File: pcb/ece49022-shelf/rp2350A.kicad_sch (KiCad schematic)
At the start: 32 parts, among them J1 USB_B_Micro, J4 SM03B-SRSS-TB, SW1 SW_Push, SW2 SW_Push, U3 W25Q128JVS, U5 RP2350_60QFN, Y1 ABM8-272-T3

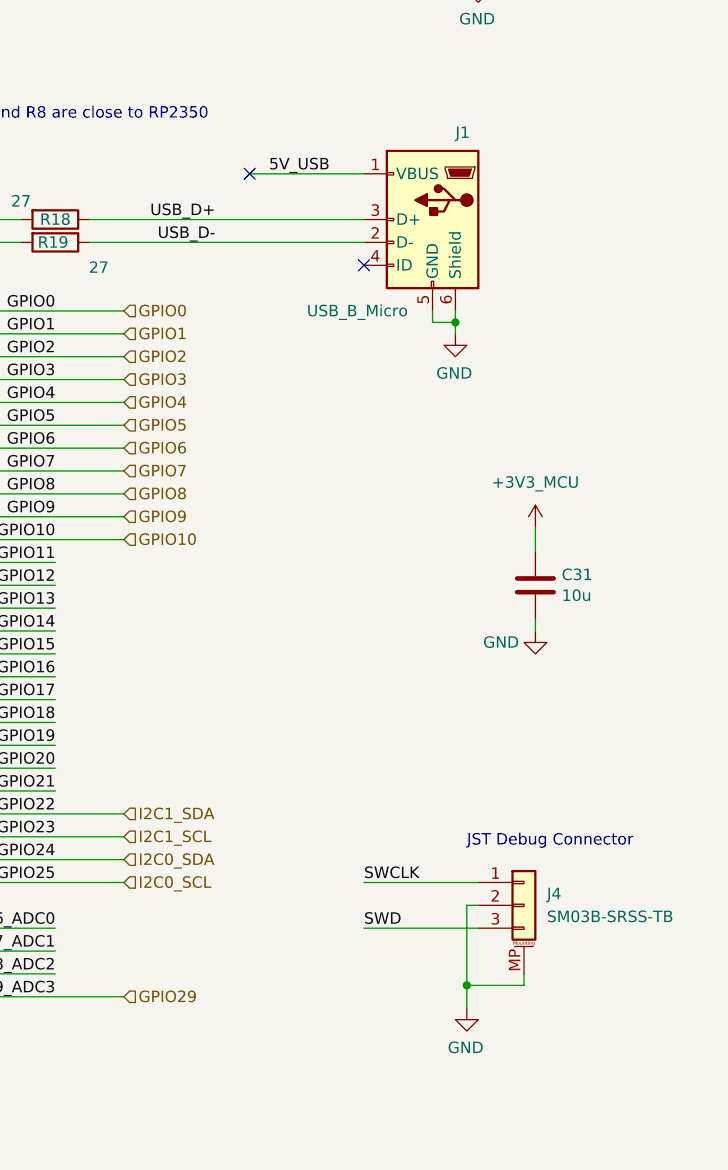
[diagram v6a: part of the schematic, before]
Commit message: new converter layout
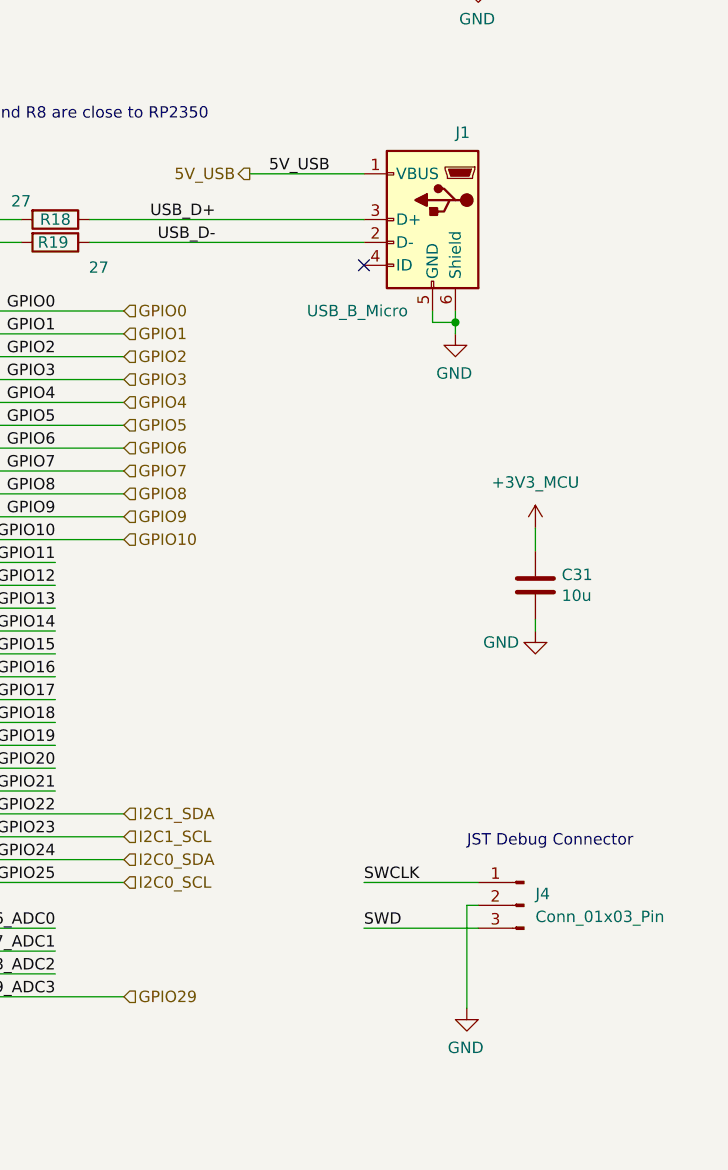
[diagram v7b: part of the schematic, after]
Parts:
- removed J4: SM03B-SRSS-TB, Connector_JST:JST_SH_SM03B-SRSS-TB_1x03-1MP_P1.00mm_Horizontal, symbol Connector_Generic_MountingPin:Conn_01x03_MountingPin
- added J4: Conn_01x03_Pin, Connector_PinHeader_2.54mm:PinHeader_1x03_P2.54mm_Vertical, symbol Connector:Conn_01x03_Pin
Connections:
- net GND: now also J4.2 (Pin_2)
- net SWCLK: now also J4.1 (Pin_1)
- net SWD: now also J4.3 (Pin_3)
- no-connect marks 2 -> 1
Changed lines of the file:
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@@
 		(color 0 0 0 0)
 	)
-	(junction
-		(at 289.56 177.8)
-		(diameter 0)
-		(color 0 0 0 0)
-	)
-	(no_connect
-		(at 265.43 87.63)
-	)
 	(no_connect
 		(at 278.13 97.79)
@@
 	(wire
 		(pts
-			(xy 289.56 177.8) (xy 289.56 180.34)
+			(xy 289.56 168.91) (xy 289.56 180.34)
 		)
 		(stroke
@@
 	(wire
 		(pts
-			(xy 289.56 168.91) (xy 289.56 177.8)
-		)
-		(stroke
-			(width 0)
-			(type default)
-		)
-	)
-	(wire
-		(pts
 			(xy 278.13 87.63) (xy 265.43 87.63)
 		)
@@
 	(wire
 		(pts
-			(xy 295.91 176.53) (xy 295.91 177.8)
-		)
-		(stroke
-			(width 0)
-			(type default)
-		)
-	)
-	(wire
-		(pts
 			(xy 233.68 52.07) (xy 245.11 52.07)
 		)
@@
 	(wire
 		(pts
-			(xy 289.56 177.8) (xy 295.91 177.8)
-		)
-		(stroke
-			(width 0)
-			(type default)
-		)
-	)
-	(wire
-		(pts
 			(xy 247.65 92.71) (xy 278.13 92.71)
 		)
@@
 		)
 	)
+	(hierarchical_label "5V_USB"
+		(shape output)
+		(at 265.43 87.63 180)
+		(effects
+			(font
+				(size 1.27 1.27)
+			)
+			(justify right)
+		)
+	)
 	(hierarchical_label "GPIO5"
 		(shape input)
@@
 	)
 	(symbol
-		(lib_id "Connector_Generic_MountingPin:Conn_01x03_MountingPin")
-		(at 295.91 168.91 0)
-		(unit 1)
-		(exclude_from_sim no)
-		(in_bom yes)
-		(on_board yes)
-		(dnp no)
-		(fields_autoplaced yes)
-		(property "Reference" "J4"
-			(at 298.45 167.64 0)
-			(effects
-				(font
-					(size 1.27 1.27)
-				)
-				(justify left)
-			)
-		)
-		(property "Value" "SM03B-SRSS-TB"
-			(at 298.45 170.18 0)
-			(effects
-				(font
-					(size 1.27 1.27)
-				)
-				(justify left)
-			)
-		)
-		(property "Footprint" "Connector_JST:JST_SH_SM03B-SRSS-TB_1x03-1MP_P1.00mm_Horizontal"
-			(at 295.91 168.91 0)
-			(effects
-				(font
-					(size 1.27 1.27)
-				)
-				(hide yes)
-			)
-		)
-		(property "Datasheet" "~"
-			(at 295.91 168.91 0)
-			(effects
-				(font
-					(size 1.27 1.27)
-				)
-				(hide yes)
-			)
-		)
-		(property "Description" ""
-			(at 295.91 168.91 0)
-			(effects
-				(font
-					(size 1.27 1.27)
-				)
-			)
-		)
-		(pin "1"
-		)
-		(pin "2"
-		)
-		(pin "3"
-		)
-		(pin "MP"
-		)
-		(instances
-			(project "ece49022-shelf"
-				(path "/cb6cb1b4-c151-4aa2-8cd7-5430288cfa02/d90a4203-0e8d-4fad-a588-f7d5681a1fb6"
-					(reference "J4")
-					(unit 1)
-				)
-			)
-		)
-	)
-	(symbol
 		(lib_name "+3V3_1")
 		(lib_id "power:+3V3")
@@
 					(unit 1)
 				)
+			)
+		)
+	)
+	(symbol
+		(lib_id "Connector:Conn_01x03_Pin")
+		(at 295.91 168.91 0)
+		(mirror y)
+		(unit 1)
+		(exclude_from_sim no)
+		(in_bom yes)
+		(on_board yes)
+		(dnp no)
+		(fields_autoplaced yes)
+		(property "Reference" "J4"
+			(at 297.18 167.6399 0)
+			(effects
+				(font
+					(size 1.27 1.27)
+				)
+				(justify right)
+			)
+		)
+		(property "Value" "Conn_01x03_Pin"
+			(at 297.18 170.1799 0)
+			(effects
+				(font
+					(size 1.27 1.27)
+				)
+				(justify right)
+			)
+		)
+		(property "Footprint" "Connector_PinHeader_2.54mm:PinHeader_1x03_P2.54mm_Vertical"
+			(at 295.91 168.91 0)
+			(effects
+				(font
+					(size 1.27 1.27)
+				)
+				(hide yes)
+			)
+		)
+		(property "Datasheet" "~"
+			(at 295.91 168.91 0)
+			(effects
+				(font
+					(size 1.27 1.27)
+				)
+				(hide yes)
+			)
+		)
+		(property "Description" "Generic connector, single row, 01x03, script generated"
+			(at 295.91 168.91 0)
+			(effects
+				(font
+					(size 1.27 1.27)
+				)
+				(hide yes)
+			)
+		)
+		(pin "1"
+		)
+		(pin "2"
+		)
+		(pin "3"
+		)
+		(instances
+			(project ""
+				(path "/cb6cb1b4-c151-4aa2-8cd7-5430288cfa02/d90a4203-0e8d-4fad-a588-f7d5681a1fb6"
+					(reference "J4")
+					(unit 1)
+				)

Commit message: stuff
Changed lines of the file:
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@@
 	(wire
 		(pts
-			(xy 228.6 143.51) (xy 243.84 143.51)
+			(xy 228.6 143.51) (xy 251.46 143.51)
 		)
 		(stroke
@@
 	(wire
 		(pts
-			(xy 228.6 151.13) (xy 243.84 151.13)
+			(xy 228.6 151.13) (xy 251.46 151.13)
 		)
 		(stroke
@@
 	(wire
 		(pts
-			(xy 228.6 148.59) (xy 243.84 148.59)
+			(xy 228.6 148.59) (xy 251.46 148.59)
 		)
 		(stroke
@@
 	(wire
 		(pts
-			(xy 228.6 156.21) (xy 243.84 156.21)
+			(xy 228.6 156.21) (xy 251.46 156.21)
 		)
 		(stroke
@@
 	(wire
 		(pts
-			(xy 228.6 146.05) (xy 243.84 146.05)
+			(xy 228.6 146.05) (xy 251.46 146.05)
 		)
 		(stroke
@@
 	(wire
 		(pts
-			(xy 228.6 153.67) (xy 243.84 153.67)
+			(xy 228.6 153.67) (xy 251.46 153.67)
 		)
 		(stroke
@@
 			)
 			(justify right bottom)
+		)
+	)
+	(hierarchical_label "GPIO17"
+		(shape input)
+		(at 251.46 146.05 0)
+		(effects
+			(font
+				(size 1.27 1.27)
+			)
+			(justify left)
+		)
+	)
+	(hierarchical_label "GPIO20"
+		(shape input)
+		(at 251.46 153.67 0)
+		(effects
+			(font
+				(size 1.27 1.27)
+			)
+			(justify left)
 		)
 	)
@@
 		)
 	)
+	(hierarchical_label "GPIO16"
+		(shape input)
+		(at 251.46 143.51 0)
+		(effects
+			(font
+				(size 1.27 1.27)
+			)
+			(justify left)
+		)
+	)
+	(hierarchical_label "GPIO18"
+		(shape input)
+		(at 251.46 148.59 0)
+		(effects
+			(font
+				(size 1.27 1.27)
+			)
+			(justify left)
+		)
+	)
 	(hierarchical_label "GPIO2"
 		(shape input)
@@
 		)
 	)
+	(hierarchical_label "GPIO19"
+		(shape input)
+		(at 251.46 151.13 0)
+		(effects
+			(font
+				(size 1.27 1.27)
+			)
+			(justify left)
+		)
+	)
 	(hierarchical_label "GPIO10"
 		(shape input)
@@
 		(effects
 			(font
+				(size 1.27 1.27)
+			)
+			(justify left)
+		)
+	)
+	(hierarchical_label "GPIO21"
+		(shape input)
+		(at 251.46 156.21 0)
+		(effects
+			(font
